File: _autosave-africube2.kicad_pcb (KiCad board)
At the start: 4 copper layers, 66 x 57 mm, 38 parts, among them IC1 ADC-20-4, J1 SMA Edge FM, J2 Conn_01x04, J3 RPi_GPIO, J4 Conn_01x02, U1 TQP7M9105, U2 SXBP-150+, U3 BA178M05FP-E2, U4 MCP3421A0T-E/CH

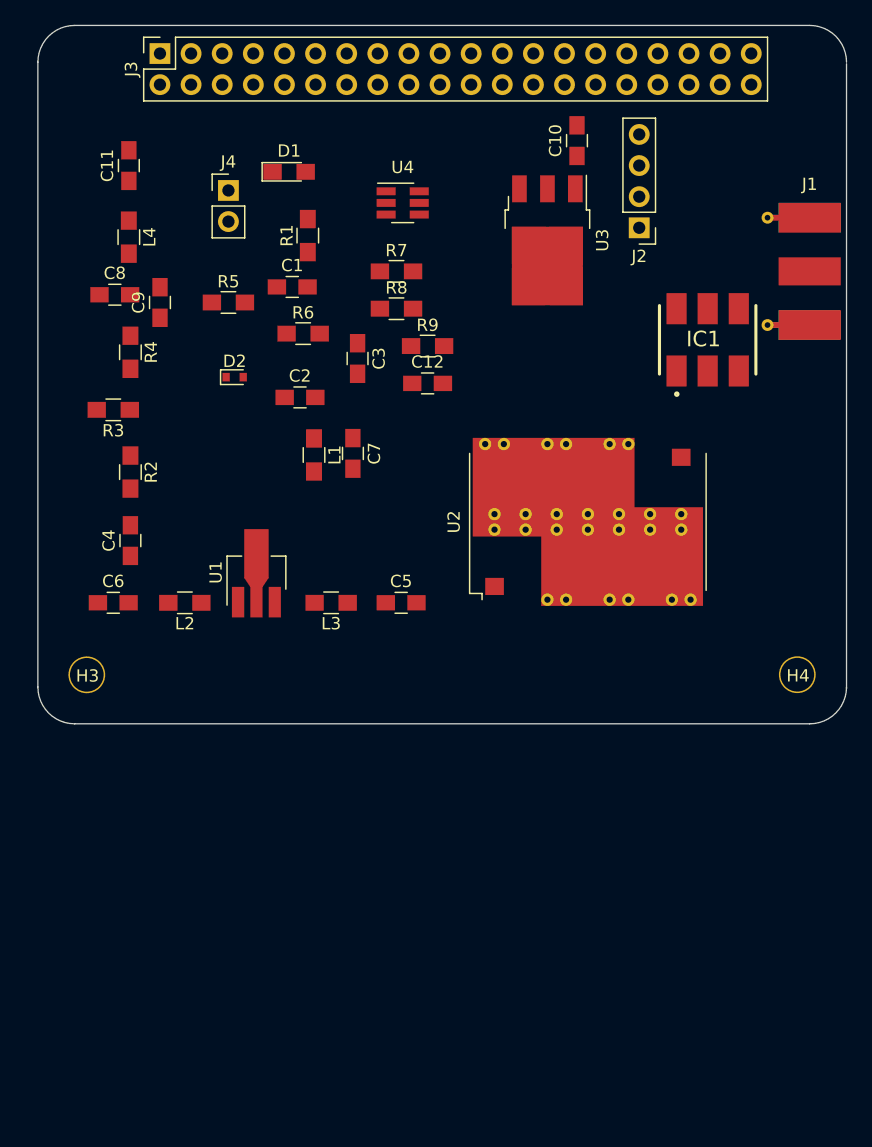
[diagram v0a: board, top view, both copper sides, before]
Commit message: Making pcb Bigger
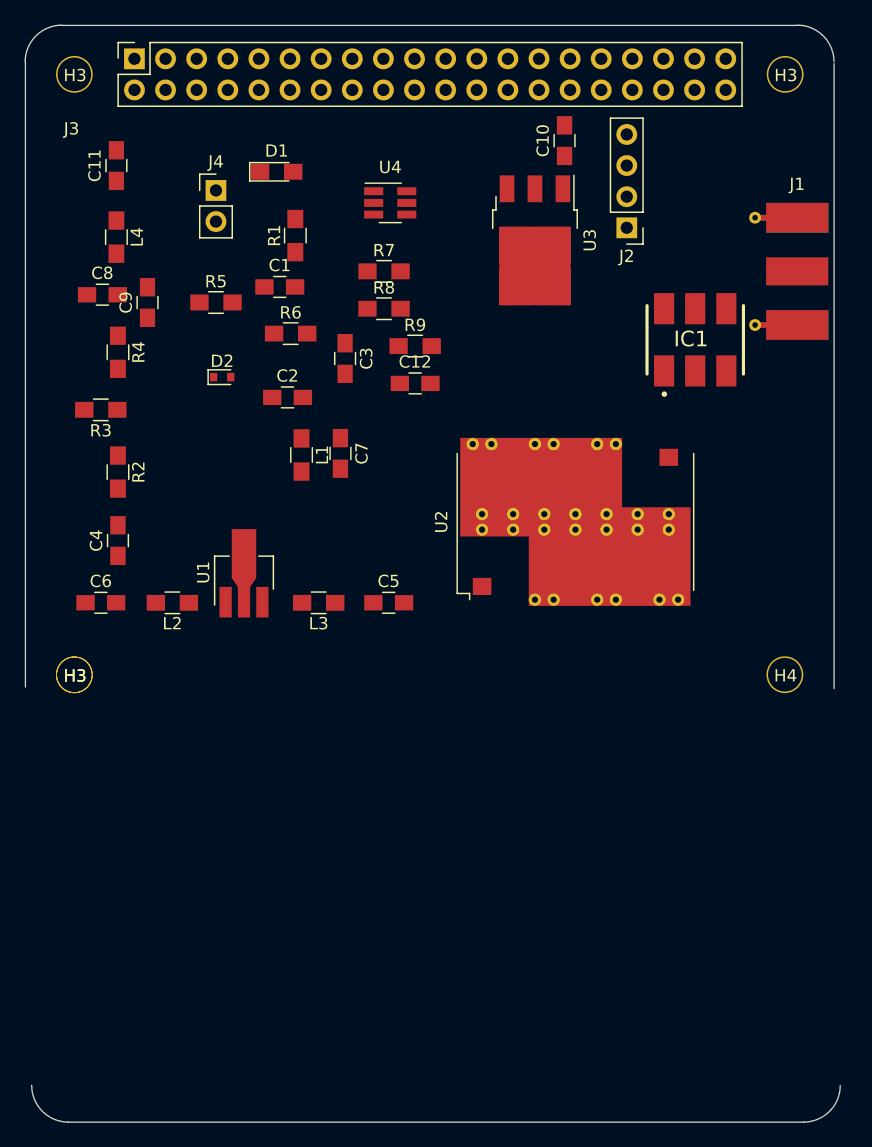
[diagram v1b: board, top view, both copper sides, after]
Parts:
- added H3: 3mm_Mounting_Hole, project_footprints:NPTH_3mm_ID, F.Cu at (139.0, 64.3)
- added H3: 3mm_Mounting_Hole, project_footprints:NPTH_3mm_ID, F.Cu at (81.0, 64.3)
- added H3: 3mm_Mounting_Hole, project_footprints:NPTH_3mm_ID, F.Cu at (81.0, 113.3)
- moved J3 2.13 mm to (85.9, 63.0)
- moved C11 1.02 mm to (84.5, 71.8)
- moved C12 1.02 mm to (108.8, 89.5)
- moved C2 1.02 mm to (98.4, 90.7)
- moved C3 1.02 mm to (103.1, 87.5)
- moved C4 1.02 mm to (84.6, 102.4)
- moved C7 1.02 mm to (102.7, 95.2)
- moved C8 1.02 mm to (83.3, 82.3)
- moved D1 1.02 mm to (97.5, 72.3)
- moved D2 1.02 mm to (93.1, 89.0)
- moved H3 1.02 mm to (81.0, 113.3)
- moved J4 1.02 mm to (92.6, 73.8)
- moved L1 1.02 mm to (99.6, 95.4)
- moved L2 1.02 mm to (89.0, 107.4)
- moved L4 1.02 mm to (84.5, 77.6)
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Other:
- board size 66 x 57 mm -> 66.5 x 89.5 mm
